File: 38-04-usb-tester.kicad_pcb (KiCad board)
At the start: 2 copper layers, 101.7 x 101.7 mm, 63 parts, among them J1 HC-USB3.0-L168-WP, J2 USB_Micro-B_KH-MICRO5P-JN, J3 USB_C_12401832E402A, J4 USB_Mini-B_U-M-M5DD-W-1, J5 Conn_01x05_Pin, J6 USB_C_12401832E402A, U1 STM32C031K6Tx

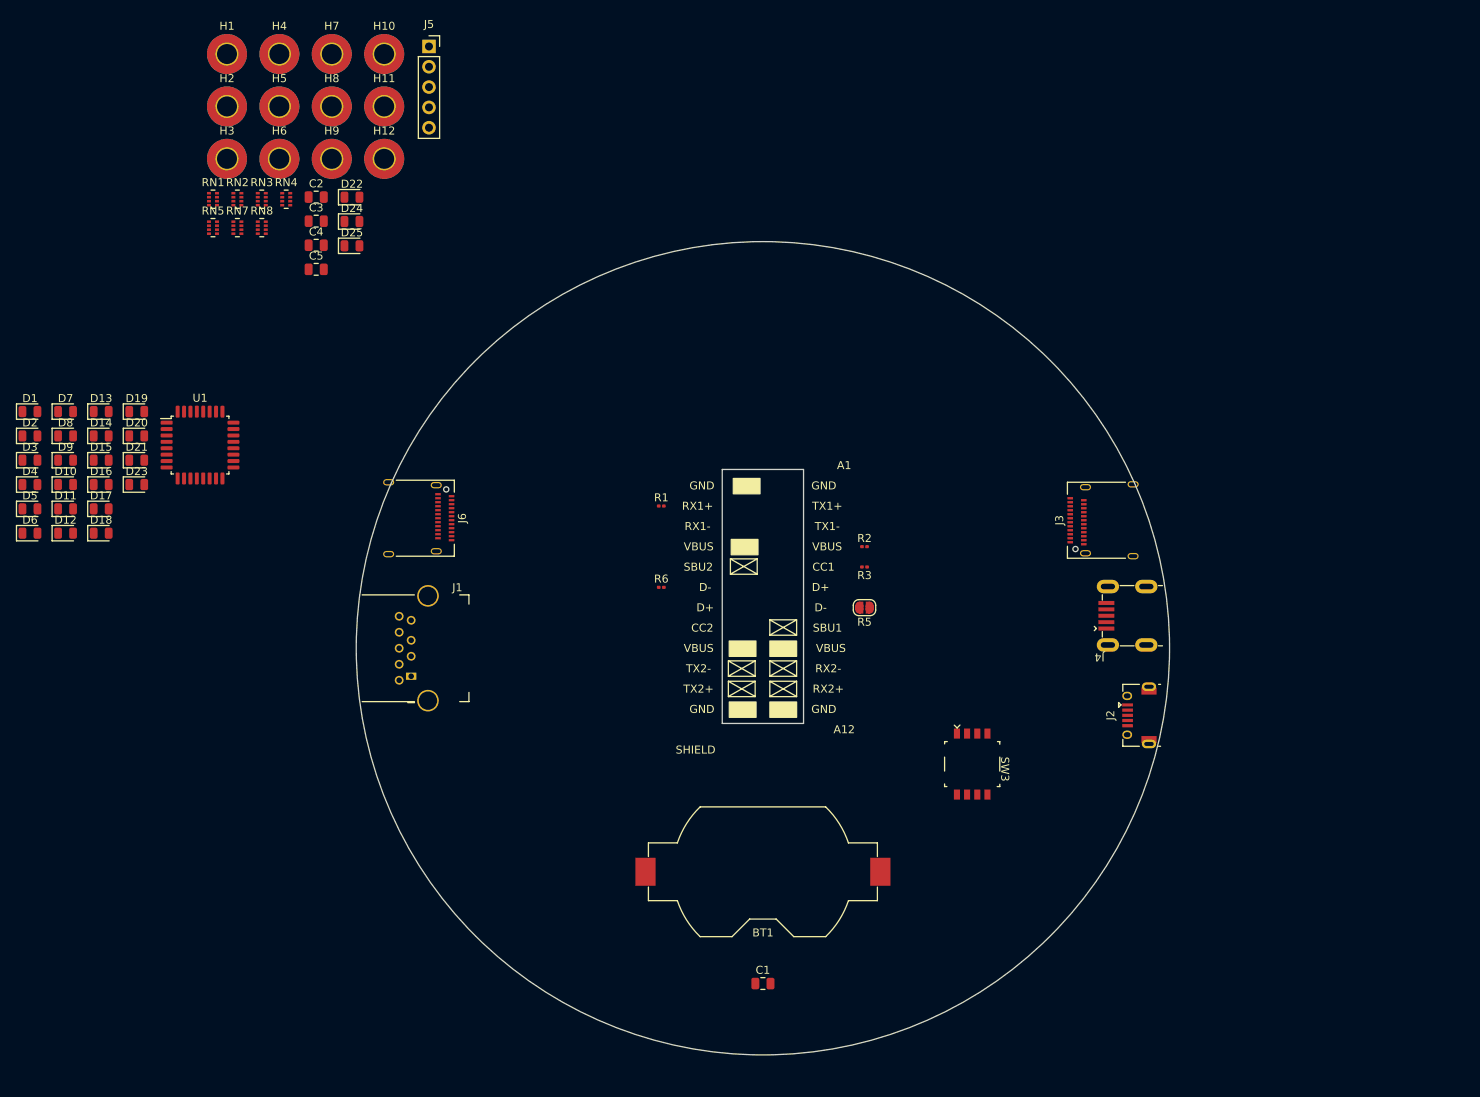
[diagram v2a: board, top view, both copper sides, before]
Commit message: edge pads and start of pcb layout
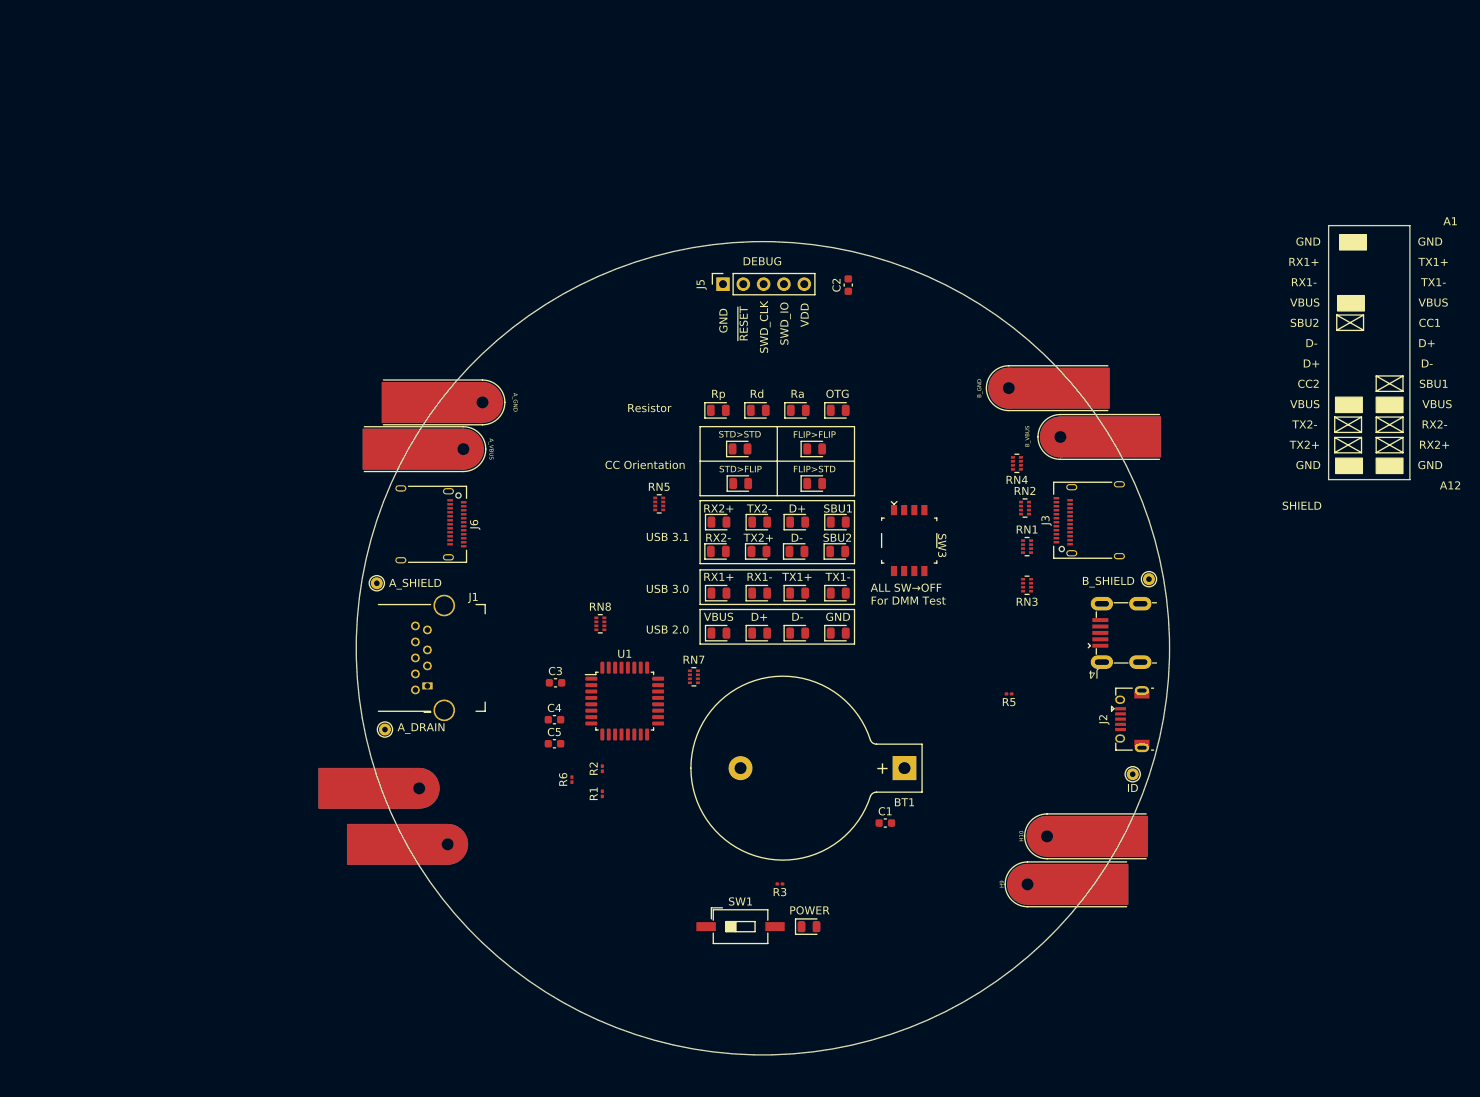
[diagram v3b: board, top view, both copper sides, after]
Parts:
- added SW1: SW_SPDT, Button_Switch_SMD:SW_DIP_SPSTx01_Slide_6.7x4.1mm_W8.61mm_P2.54mm_LowProfile, F.Cu at (152.1, 145.3)
- BT1: footprint Battery:BatteryHolder_Keystone_1058_1x2032 -> Battery:BatteryHolder_Keystone_103_1x20mm
- C1, C2, C3, C4, C5: footprint Capacitor_SMD:C_0805_2012Metric -> Capacitor_SMD:C_0603_1608Metric
- D1, D13, D9: value SSRx2+_D -> YLW
- D10, D2: value SSRx1+_D -> YLW
- D11, D3: value SSRx1-_D -> YLW
- D12, D23, D8: value SSRx2-_D -> YLW
- D14: value GND_D -> YLW
- D15: value VBUS_LED_D -> YLW
- D16: value CC_NORM_D -> YLW
- D17: value CC_REV_D -> YLW
- D18: value Rp_D -> YLW
- D19: value Rd_D -> YLW
- D20: value Ra_D -> YLW
- D21: value OTG_D -> YLW
- D22: value Power -> YLW
- D24: value CC_bb_D -> YLW
- D25: value CC_ba_D -> YLW
- D4: value SSTx2-_D -> YLW
- D5: value SSTx2+_D -> YLW
- D6: value SSTx1+_D -> YLW
- D7: value SSTx1-_D -> YLW
- H1: value B_CC1 -> B_VBUS; footprint MountingHole:MountingHole_2.5mm_Pad_TopBottom -> 01-UserLibary:Connector_Pad_Edge_Oval_5mm_Extended
- H10: value A_GND -> B_CC1; footprint MountingHole:MountingHole_2.5mm_Pad_TopBottom -> 01-UserLibary:Connector_Pad_Edge_Oval_5mm_Extended
- H11: value B_VBUS -> A_CC1; footprint MountingHole:MountingHole_2.5mm_Pad_TopBottom -> 01-UserLibary:Connector_Pad_Edge_Oval_5mm_Extended; moved to B.Cu
- H12: value B_GND -> A_CC2; footprint MountingHole:MountingHole_2.5mm_Pad_TopBottom -> 01-UserLibary:Connector_Pad_Edge_Oval_5mm_Extended; moved to B.Cu
- H2: value B_CC2 -> A_VBUS; footprint MountingHole:MountingHole_2.5mm_Pad_TopBottom -> 01-UserLibary:Connector_Pad_Edge_Oval_5mm_Extended
- H3: value A_CC2 -> B_GND; footprint MountingHole:MountingHole_2.5mm_Pad_TopBottom -> 01-UserLibary:Connector_Pad_Edge_Oval_5mm_Extended
- H4: value A_CC1 -> A_GND; footprint MountingHole:MountingHole_2.5mm_Pad_TopBottom -> 01-UserLibary:Connector_Pad_Edge_Oval_5mm_Extended
- H5, H6, H7, H8: footprint MountingHole:MountingHole_2.5mm_Pad_TopBottom -> TestPoint:TestPoint_THTPad_D1.5mm_Drill0.7mm
- H9: value A_VBUS -> B_CC2; footprint MountingHole:MountingHole_2.5mm_Pad_TopBottom -> 01-UserLibary:Connector_Pad_Edge_Oval_5mm_Extended
- R3: value 10k -> 1K
- R5: value 2k -> 2K; footprint Jumper:SolderJumper-2_P1.3mm_Open_RoundedPad1.0x1.5mm -> Resistor_SMD:R_0201_0603Metric
- RN1, RN2, RN3, RN4, RN5, RN7, RN8: value 10K -> 1K
- SW3: value ~ -> ZX-1.27BM-4PSMD
- moved H10 136.6 mm to (203.0, 134.0), turned to 90 degrees
- moved H5 135.4 mm to (201.2, 126.2)
- moved H9 134.6 mm to (200.6, 140.0), turned to 90 degrees
- moved H1 126.1 mm to (204.7, 84.1), turned to 90 degrees
- moved H6 120.7 mm to (203.2, 101.9)
- moved H3 113.9 mm to (198.2, 78.0), turned to 90 degrees
- moved RN1 110.6 mm to (188.0, 97.8)
- moved D22 107.6 mm to (160.7, 145.3)
- moved RN3 107.1 mm to (188.0, 102.6), turned to 180 degrees
- moved RN2 105.8 mm to (187.7, 93.0)
- moved D7 99.2 mm to (164.4, 103.6)
- moved RN4 97.1 mm to (186.7, 87.4), turned to 180 degrees
- moved D12 96.6 mm to (164.4, 94.7)
- moved D6 96.2 mm to (159.3, 103.6)
- moved D14 95.4 mm to (164.4, 108.6)
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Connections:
- net /A_SBU1_D renamed /A_SBU1
- D8 pad 2: /A_D1+_D -> /A_D1+
- D9 pad 2: /A_D1-_D -> /A_D1-
- H1 pad 1: /B_CC1_SENS -> /B_VBUS_A4
- H10 pad 1: /A_GND -> /B_CC1_SENS
- H11 pad 1: /B_VBUS_A4 -> /A_CC1
- H12 pad 1: /B_GND_B1 -> /A_CC2
- H2 pad 1: /B_CC2_SENS -> /A_VBUS
- H3 pad 1: /A_CC2 -> /B_GND_B1
- H4 pad 1: /A_CC1 -> /A_GND
- H9 pad 1: /A_VBUS -> /B_CC2_SENS
- J6 pad A6: /A_D1+_D -> /A_D1+
- J6 pad A7: /A_D1-_D -> /A_D1-
- R5 pad 2: Net-(JP3-B) -> Net-(R5-Pad2)
- RN3 pad 1: /B_D1- -> /B_SSRTx1+
- RN3 pad 2: /B_D1+ -> /B_SSRx1-
- RN3 pad 3: /B_SSRx1- -> /B_D1+
- RN3 pad 4: /B_SSRTx1+ -> /B_D1-
- RN4 pad 1: /B_SSRx2+ -> /B_SBU1
- RN4 pad 2: /B_SSRx2- -> unconnected-(RN4-R2.1-Pad2)
- RN4 pad 3: unconnected-(RN4-R3.1-Pad3) -> /B_SSRx2-
- RN4 pad 4: /B_SBU1 -> /B_SSRx2+
- RN4 pad 7: VCC -> unconnected-(RN4-R2.2-Pad7)
- RN5 pad 1: unconnected-(RN5-R1.1-Pad1) -> Net-(D17-A)
- RN5 pad 2: unconnected-(RN5-R2.1-Pad2) -> Net-(D16-A)
- RN5 pad 5: /CC_bb -> /CC_aa
- RN5 pad 6: /CC_ba -> /CC_ab
- RN5 pad 7: unconnected-(RN5-R2.2-Pad7) -> /CC_bb
- RN5 pad 8: unconnected-(RN5-R1.2-Pad8) -> /CC_ba
- RN7 pad 1: Net-(D17-A) -> unconnected-(RN7-R1.1-Pad1)
- RN7 pad 2: Net-(D16-A) -> unconnected-(RN7-R2.1-Pad2)
- RN7 pad 7: /CC_aa -> unconnected-(RN7-R2.2-Pad7)
- RN7 pad 8: /CC_ab -> unconnected-(RN7-R1.2-Pad8)
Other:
- board size 101.7 x 101.7 mm -> 131.7 x 103.7 mm
- board text added: "ALL SW→OFF For DMM Test"
- board text added: "CC Orientation"
- board text added: "DEBUG"
- board text added: "FLIP>FLIP"
- board text added: "FLIP>STD"
- board text added: "OTG"
- board text added: "POWER"
- board text added: "Ra"
- board text added: "Rd"
- board text added: "Resistor"
- board text added: "Rp"
- board text added: "STD>FLIP"
- board text added: "STD>STD"
- board text added: "SWD_CLK"
- board text added: "SWD_IO"
- board text added: "USB 2.0"
- board text added: "USB 3.0"
- board text added: "USB 3.1"
- board text added: "VDD"
- board text added: "~{RESET}"

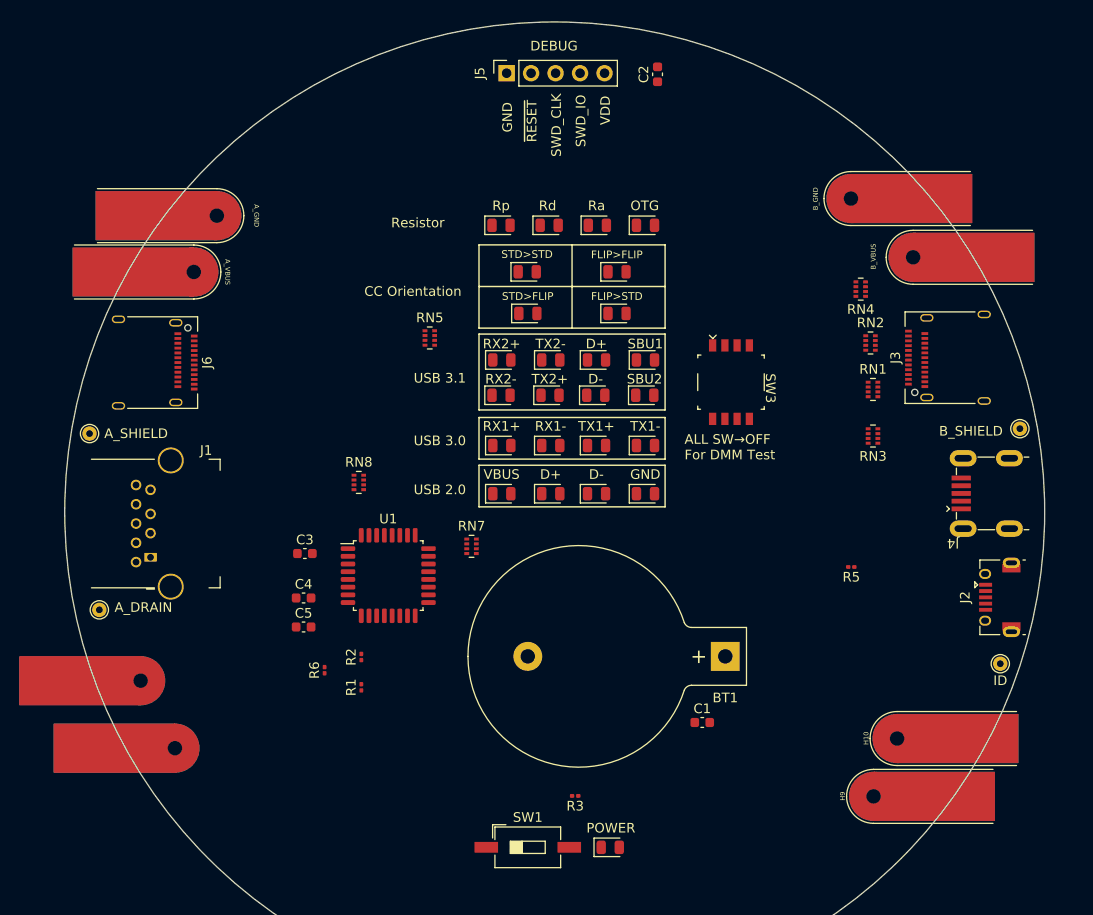
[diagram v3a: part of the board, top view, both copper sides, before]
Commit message: pcb layout - cleanup, DNP decisions
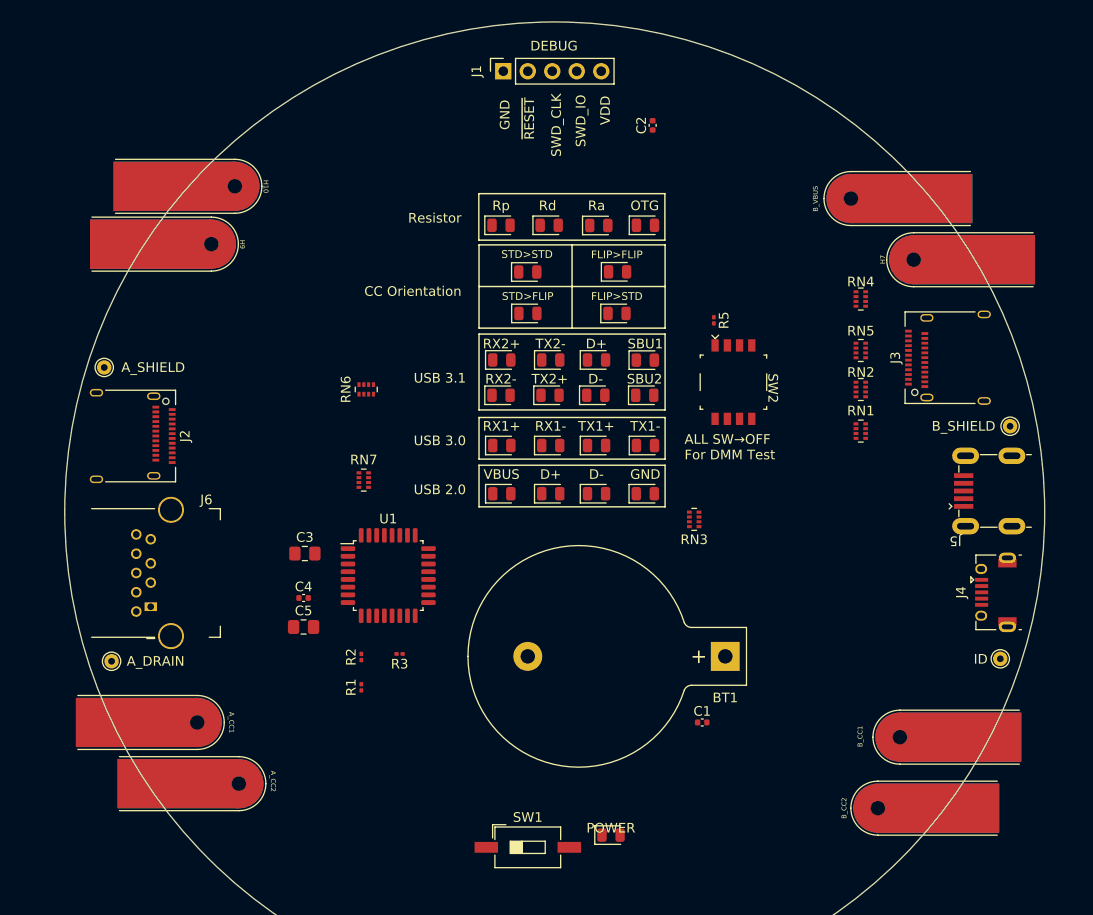
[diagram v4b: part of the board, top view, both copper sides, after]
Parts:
- removed R6: 10k, Resistor_SMD:R_0201_0603Metric
- removed RN8: 1K, Resistor_SMD:R_Array_Concave_4x0402
- removed SW3: ZX-1.27BM-4PSMD, 01-UserLibary:SW-DIP-4P_P1.27mm_SMD-2x4
- added RN6: 1K, Resistor_SMD:R_Array_Concave_4x0402, F.Cu at (135.4, 97.8)
- added SW2: ZX-1.27BM-4PSMD, 01-UserLibary:SW-DIP-4P_P1.27mm_SMD-2x4, F.Cu at (173.5, 97.0)
- BT1: value Battery -> CR2032
- C1: value 1uF -> 100n; footprint Capacitor_SMD:C_0603_1608Metric -> Capacitor_SMD:C_0402_1005Metric
- C2, C4: footprint Capacitor_SMD:C_0603_1608Metric -> Capacitor_SMD:C_0402_1005Metric
- C3: value 100n -> 4u7; footprint Capacitor_SMD:C_0603_1608Metric -> Capacitor_SMD:C_0805_2012Metric_Pad1.18x1.45mm_HandSolder
- C5: value 4u7 -> 1uF; footprint Capacitor_SMD:C_0603_1608Metric -> Capacitor_SMD:C_0805_2012Metric_Pad1.18x1.45mm_HandSolder
- H1: value B_VBUS -> B_CC1
- H10: value B_CC1 -> A_VBUS
- H11: value A_CC1 -> ID; footprint 01-UserLibary:Connector_Pad_Edge_Oval_5mm_Extended -> TestPoint:TestPoint_THTPad_D1.5mm_Drill0.7mm; moved to F.Cu
- H12: value A_CC2 -> A_DRAIN; footprint 01-UserLibary:Connector_Pad_Edge_Oval_5mm_Extended -> TestPoint:TestPoint_THTPad_D1.5mm_Drill0.7mm; moved to F.Cu
- H2: value A_VBUS -> B_CC2
- H3: value B_GND -> B_VBUS
- H4: value A_GND -> A_CC1
- H5: value ID -> A_CC2; footprint TestPoint:TestPoint_THTPad_D1.5mm_Drill0.7mm -> 01-UserLibary:Connector_Pad_Edge_Oval_5mm_Extended
- H6: value B_SHIELD -> A_SHIELD
- H7: value A_SHIELD -> B_GND; footprint TestPoint:TestPoint_THTPad_D1.5mm_Drill0.7mm -> 01-UserLibary:Connector_Pad_Edge_Oval_5mm_Extended
- H8: value A_DRAIN -> B_SHIELD
- H9: value B_CC2 -> A_GND
- J1: value HC-USB3.0-L168-WP -> Conn_1x05; footprint 01-UserLibary:USB_A_Hong-Cheng_HC-USB3.0-L168-WP_THT-9-2MP_P2.0mm -> Connector_PinSocket_2.54mm:PinSocket_1x05_P2.54mm_Vertical
- J2: value USB_Micro-B_KH-MICRO5P-JN -> USB_C_12401832E402A; footprint 01-UserLibary:USB_Micro-B_Kinghelm-KH-MICRO5P-JN -> 01-UserLibary:USB_C_Receptacle_Amphenol_12401832E402A
- J4: value USB_Mini-B_U-M-M5DD-W-1 -> USB_Micro-B_KH-MICRO5P-JN; footprint 01-UserLibary:USB_Mini-B_Korean-Hroparts_U-M-M5DD-W-1_SMD-5-4MP -> 01-UserLibary:USB_Micro-B_Kinghelm-KH-MICRO5P-JN
- J5: value Conn_01x05_Pin -> USB_Mini-B_U-M-M5DD-W-1; footprint Connector_PinSocket_2.54mm:PinSocket_1x05_P2.54mm_Vertical -> 01-UserLibary:USB_Mini-B_Korean-Hroparts_U-M-M5DD-W-1_SMD-5-4MP
- J6: value USB_C_12401832E402A -> USB3_A_HC-USB3.0-L168-WP; footprint 01-UserLibary:USB_C_Receptacle_Amphenol_12401832E402A -> 01-UserLibary:USB3_A_Hong-Cheng_HC-USB3.0-L168-WP_THT-9-2MP_P2.0mm
- R3: value 1K -> 10k
- moved H2 111.0 mm to (201.0, 141.2), turned to 90 degrees
- moved H10 109.9 mm to (109.2, 76.7), turned to -90 degrees
- moved H9 109.9 mm to (106.8, 82.7), turned to -90 degrees
- moved H11 101.8 mm to (201.2, 125.7), turned to 180 degrees
- moved H7 99.7 mm to (204.7, 84.3), turned to 90 degrees
- moved H8 96.4 mm to (202.2, 101.6)
- moved H6 95.2 mm to (108.2, 95.5)
- moved J2 93.6 mm to (110.2, 102.6), turned to -90 degrees
- moved H5 92.4 mm to (109.6, 138.7), turned to -90 degrees
- moved D22 64.8 mm to (154.4, 80.8)
- moved J5 64.2 mm to (197.4, 108.3), turned to 180 degrees
- moved J1 60.4 mm to (149.6, 64.8)
- moved H4 52.6 mm to (105.3, 132.3)
- moved D1 50.6 mm to (160.8, 144.0)
- moved H1 49.8 mm to (203.3, 133.9)
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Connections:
- C1 pad 1: Net-(BT1-+) -> /~{RESET}
- C3 pad 1: /~{RESET} -> GND
- C3 pad 2: GND -> VCC
- C5 pad 1: GND -> Net-(BT1-+)
- C5 pad 2: VCC -> GND
- D1 pad 2: /A_SSRx2+ -> /PWR_LED
- D10 pad 2: /A_D2- -> /A_SSRx1-
- D11 pad 2: /A_D2+ -> /A_SSTx1-
- D12 pad 2: /A_SBU1 -> Net-(D12-A)
- D13 pad 2: /A_SBU2 -> /A_D1+
- D14 pad 2: Net-(D14-A) -> /A_SBU1
- D18 pad 2: Net-(D18-A) -> /A_D1-
- D19 pad 2: Net-(D19-A) -> /A_SBU2
- D2 pad 2: /A_SSRx1+ -> /A_SSRx2-
- D20 pad 2: Net-(D20-A) -> /A_D2-
- D21 pad 1: /ID -> GND
- D23 pad 2: /A_SSRx2- -> /A_D2+
- D25 pad 1: GND -> /ID
- D3 pad 2: /A_SSRx1- -> /A_SSTx2-
- D4 pad 2: /A_SSTx2- -> /A_SSRx2+
- D6 pad 2: /A_SSTx1+ -> Net-(D6-A)
- D7 pad 2: /A_SSTx1- -> /A_SSRx1+
- D8 pad 2: /A_D1+ -> /A_SSTx1+
- D9 pad 2: /A_D1- -> Net-(D9-A)
- H1 pad 1: /B_VBUS_A4 -> /B_CC1_SENS
- H10 pad 1: /B_CC1_SENS -> /A_VBUS
- H11 pad 1: /A_CC1 -> /ID
- H12 pad 1: /A_CC2 -> /A_DRAIN
- H2 pad 1: /A_VBUS -> /B_CC2_SENS
- H3 pad 1: /B_GND_B1 -> /B_VBUS_A4
- H4 pad 1: /A_GND -> /A_CC1
- H5 pad 1: /ID -> /A_CC2
- H6 pad 1: /B_SHIELD -> /A_SHIELD
- H7 pad 1: /A_SHIELD -> /B_GND_B1
- H8 pad 1: /A_DRAIN -> /B_SHIELD
- H9 pad 1: /B_CC2_SENS -> /A_GND
- J1 pad 1: /A_VBUS -> GND
- J1 pad 2: /A_D1-_D -> /~{RESET}
- J1 pad 3: /A_D1+_D -> /SWCLK_BOOT0
- J1 pad 4: /A_GND -> /SWDIO
- J1 pad 5: /A_SSRx1- -> VCC
- J5 pad 1: GND -> /B_VBUS_A4
- J5 pad 2: /~{RESET} -> /B_D1-
- J5 pad 3: /SWCLK_BOOT0 -> /B_D1+
- J5 pad 4: /SWDIO -> /ID
- J5 pad 5: VCC -> GND
- R1 pad 1: /CC2_CTRL -> /A_VBUS_SENS
- R1 pad 2: /B_CC2_SENS -> GND
- R3 pad 1: VCC -> /CC2_CTRL
- R3 pad 2: Net-(D22-A) -> /B_CC2_SENS
- RN1 pad 7: unconnected-(RN1-R2.2-Pad7) -> /PWR_LED
- RN2 pad 1: VCC -> /B_SSRTx1+
- RN2 pad 2: VCC -> /B_SSRx1-
- RN2 pad 3: VCC -> /B_D1+
- RN2 pad 4: VCC -> /B_D1-
- RN2 pad 5: /B_D2- -> VCC
- RN2 pad 6: /B_D2+ -> VCC
- RN2 pad 7: /B_SSTx2- -> VCC
- RN2 pad 8: /B_SSTx2+ -> VCC
- RN3 pad 1: /B_SSRTx1+ -> unconnected-(RN3-R1.1-Pad1)
- RN3 pad 2: /B_SSRx1- -> unconnected-(RN3-R2.1-Pad2)
- RN3 pad 3: /B_D1+ -> Net-(D9-A)
- RN3 pad 4: /B_D1- -> Net-(D6-A)
- RN3 pad 5: VCC -> /GND_LED
- RN3 pad 6: VCC -> /VBUS_LED
- RN3 pad 7: VCC -> unconnected-(RN3-R2.2-Pad7)
- RN3 pad 8: VCC -> unconnected-(RN3-R1.2-Pad8)
- RN4 pad 1: /B_SBU1 -> VCC
- RN4 pad 2: unconnected-(RN4-R2.1-Pad2) -> VCC
- RN4 pad 3: /B_SSRx2- -> VCC
- RN4 pad 4: /B_SSRx2+ -> VCC
- RN4 pad 5: VCC -> /B_D2-
- RN4 pad 6: VCC -> /B_D2+
- RN4 pad 7: unconnected-(RN4-R2.2-Pad7) -> /B_SSTx2-
- RN4 pad 8: VCC -> /B_SSTx2+
- RN5 pad 1: Net-(D17-A) -> /B_SBU1
- RN5 pad 2: Net-(D16-A) -> unconnected-(RN5-R2.1-Pad2)
- RN5 pad 3: Net-(D25-A) -> /B_SSRx2-
- RN5 pad 4: Net-(D24-A) -> /B_SSRx2+
- RN5 pad 5: /CC_aa -> VCC
- RN5 pad 6: /CC_ab -> VCC
- RN5 pad 7: /CC_bb -> unconnected-(RN5-R2.2-Pad7)
- RN5 pad 8: /CC_ba -> VCC
- RN7 pad 1: unconnected-(RN7-R1.1-Pad1) -> Net-(D25-A)
- RN7 pad 2: unconnected-(RN7-R2.1-Pad2) -> Net-(D24-A)
- RN7 pad 3: Net-(D15-A) -> Net-(D22-A)
- RN7 pad 4: Net-(D14-A) -> Net-(D21-A)
- RN7 pad 5: /GND_LED -> /CC_Rp_LED
- RN7 pad 6: /VBUS_LED -> /CC_Rd_LED
- RN7 pad 7: unconnected-(RN7-R2.2-Pad7) -> /E_MARKER_LED
- RN7 pad 8: unconnected-(RN7-R1.2-Pad8) -> VCC
- U1 pad 4: VCC -> VDD
